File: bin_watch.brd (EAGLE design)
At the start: 39.2 x 30.1 mm, 110 parts, among them J1 USB3100-XX-X_REVB, Q1 32.768kHz, T1 2N7002BKV, T2 2N7002BKV, T3 2N7002BKV, T4 2N7002BKV, T5 PMDT670UPE, T6 PMDT670UPE, T7 PMDT670UPE, U1 MCP73831T-2ACI/OT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

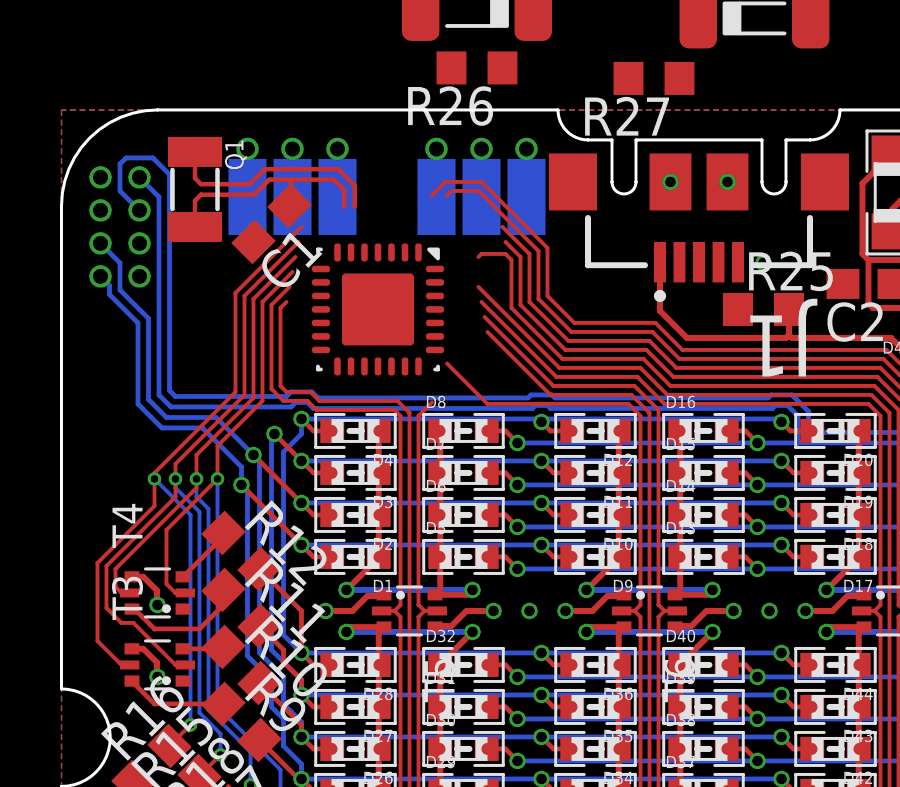
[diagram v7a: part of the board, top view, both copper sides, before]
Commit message: IO wired, USB disconnected
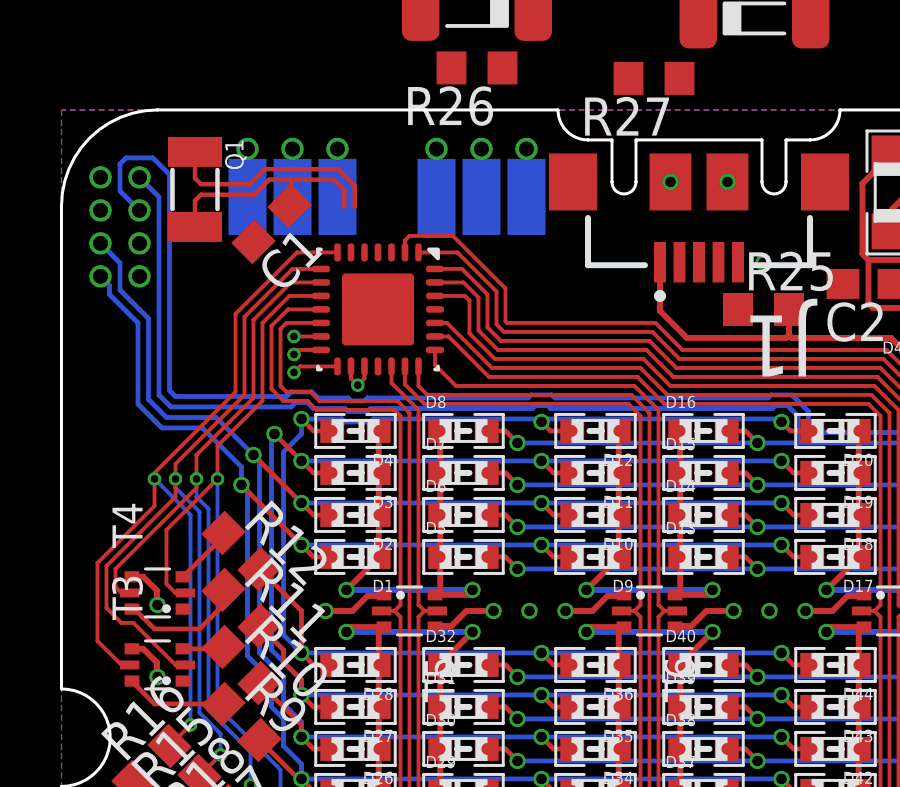
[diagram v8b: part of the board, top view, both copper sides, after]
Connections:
- removed net N$10: U$5.26
- removed net N$11: U$5.27
- removed net N$12: U$5.1
- removed net N$13: U$5.7
- removed net N$14: U$5.8
- removed net N$15: U$5.9
- removed net N$16: U$5.10
- removed net N$17: U$5.11
- removed net N$18: U$5.12
- removed net N$4: U$5.19
- removed net N$5: U$5.20
- removed net N$6: U$5.21
- removed net N$7: U$5.22
- removed net N$8: U$5.23
- removed net N$9: U$5.24
- net BTN1: now also U$5.12
- net BTN2: now also U$5.21
- net BTN3: now also U$5.24
- net G_BLOCK0: now also U$5.11
- net G_BLOCK1: now also U$5.20
- net G_BLOCK2: now also U$5.23
- net G_BLOCK3: now also U$5.19
- net G_BLOCK4: now also U$5.22
- net G_BLOCK5: now also U$5.26
- net G_LIGHT0: now also U$5.1
- net G_LIGHT1: now also U$5.2
- net G_LIGHT2: now also U$5.27
- net G_LIGHT3: now also U$5.28
- net G_LIGHT4: now also U$5.8
- net G_LIGHT5: now also U$5.7
- net G_LIGHT6: now also U$5.10
- net G_LIGHT7: now also U$5.9
- net N$2: no longer U$5.2
- net N$3: no longer U$5.28
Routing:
- net BTN2: track 27.0 -> 29.2 mm
- net G_BLOCK1: track 40.4 -> 42.1 mm
- net SCK: track 0.00 -> 1.53 mm, vias 0 -> 1
- net G_LIGHT2: track 37.5 -> 39.0 mm
- net G_BLOCK4: track 40.5 -> 42.0 mm
- net VCC: track 28.1 -> 29.6 mm, vias 10 -> 11
- net G_BLOCK3: track 27.8 -> 29.2 mm
- net G_LIGHT3: track 44.0 -> 45.4 mm
- net G_BLOCK2: track 42.1 -> 43.1 mm
- net MISO: track 0.00 -> 0.96 mm, vias 0 -> 1
- net BTN3: track 35.9 -> 36.8 mm
- net MOSI: track 0.00 -> 0.90 mm, vias 0 -> 1
- net G_BLOCK5: track 43.8 -> 44.3 mm
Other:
- board text removed: "ISP"
- board text removed: "RST"
